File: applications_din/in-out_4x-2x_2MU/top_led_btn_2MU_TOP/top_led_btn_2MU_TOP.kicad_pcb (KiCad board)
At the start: 2 copper layers, 32 x 42 mm, 17 parts, among them J2 Conn_01x08_Pin, SW1 SW_PROG, SW2 SW_OUTA, SW3 SW_OUTB

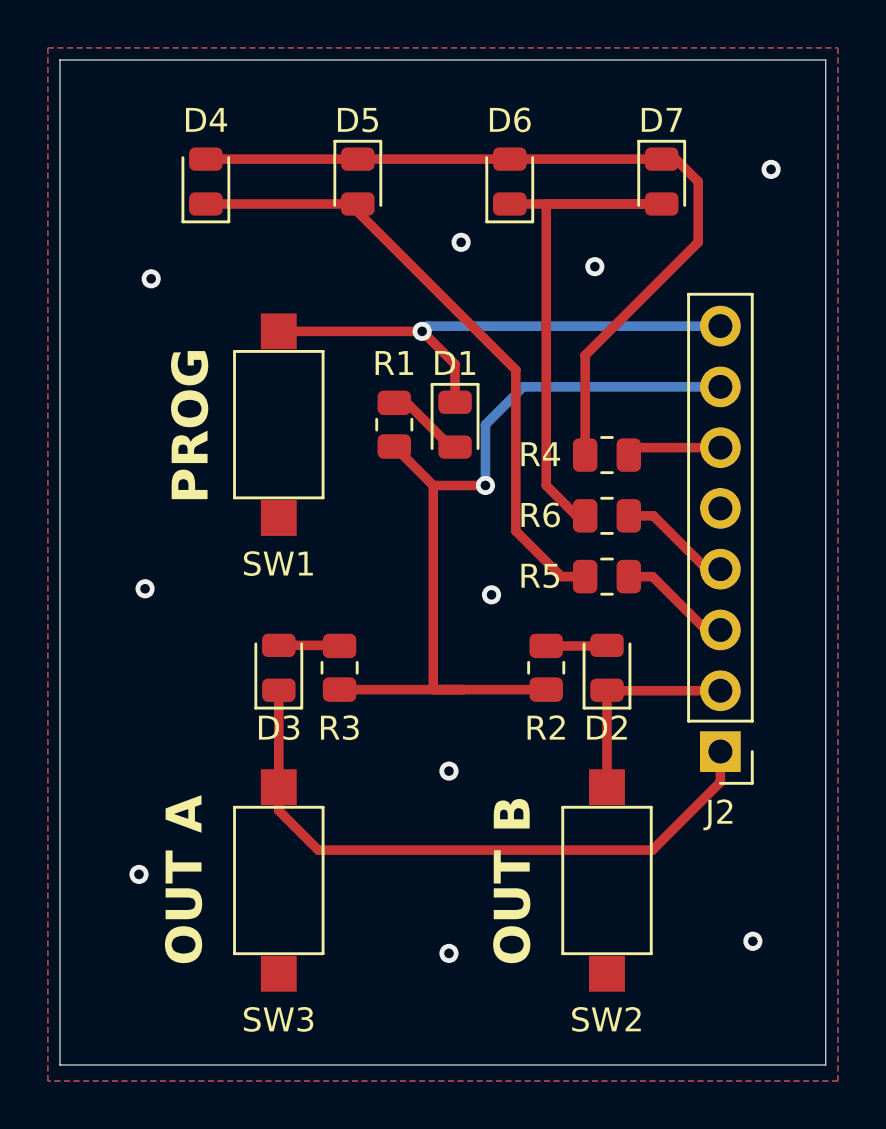
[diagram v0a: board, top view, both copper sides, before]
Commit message: properly rename 4in-2out application & top projects
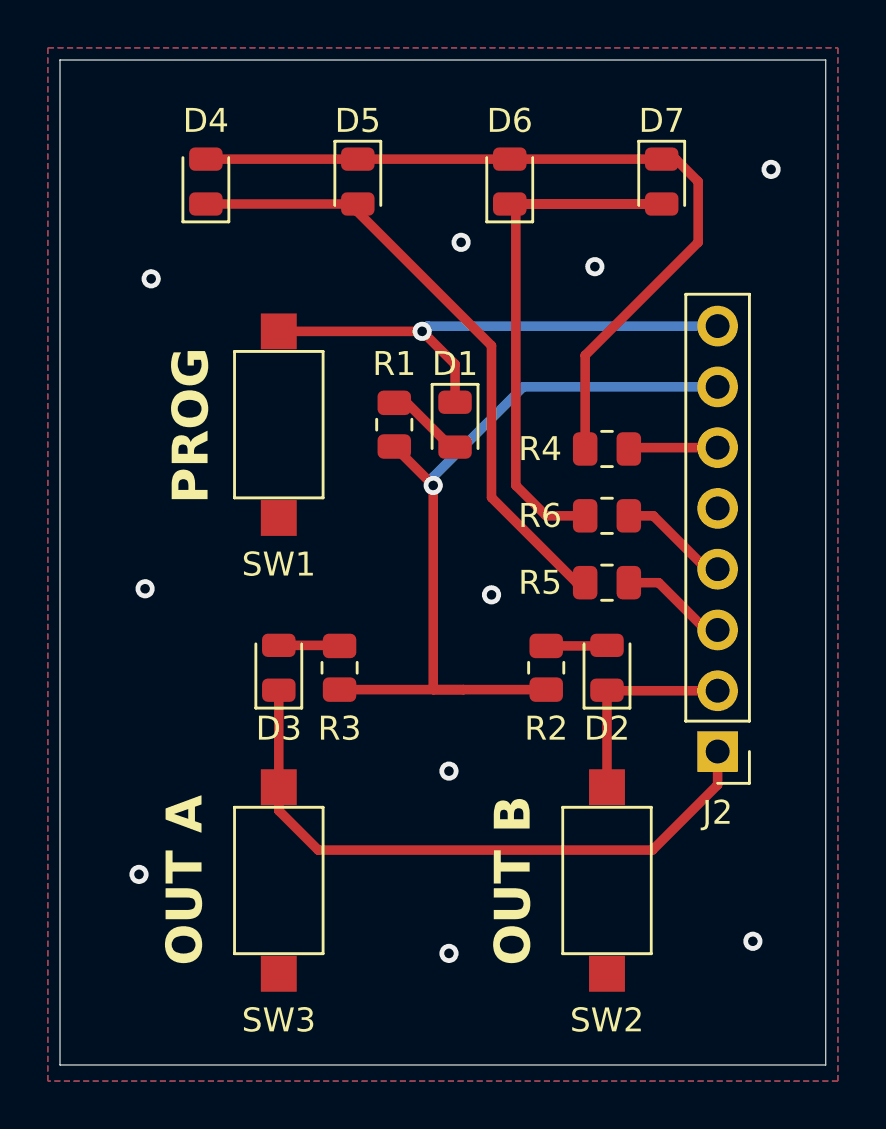
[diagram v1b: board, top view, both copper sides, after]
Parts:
- moved R4 0.25 mm to (121.9, 89.9)
- moved R5 0.25 mm to (121.9, 95.5)
- moved J2 0.12 mm to (126.5, 102.6)
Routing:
- net Net-(D6-K): track 25.1 -> 27.6 mm
- net +3V3: track 35.9 -> 34.5 mm
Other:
- board text added: "switch alternativ PTS636 SKG25J SMTR LFS https://eu.mouser.com/ProductDetail/CK/PTS636-SKG25J-SMTR-LFS"
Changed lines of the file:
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@@
 	(footprint "Resistor_SMD:R_0805_2012Metric"
 		(layer "F.Cu")
-		(at 121.92 90.17)
+		(at 121.92 89.916)
 		(descr "Resistor SMD 0805 (2012 Metric), square (rectangular) end terminal, IPC_7351 nominal, (Body size source: IPC-SM-782 page 72, https://www.pcb-3d.com/wordpress/wp-content/uploads/ipc-sm-782a_amendment_1_and_2.pdf), generated with kicad-footprint-generator")
 		(tags "resistor")
@@
 	(footprint "Resistor_SMD:R_0805_2012Metric"
 		(layer "F.Cu")
-		(at 121.92 95.25 180)
+		(at 121.92 95.504 180)
 		(descr "Resistor SMD 0805 (2012 Metric), square (rectangular) end terminal, IPC_7351 nominal, (Body size source: IPC-SM-782 page 72, https://www.pcb-3d.com/wordpress/wp-content/uploads/ipc-sm-782a_amendment_1_and_2.pdf), generated with kicad-footprint-generator")
 		(tags "resistor")
@@
 	(footprint "Connector_PinHeader_2.54mm:PinHeader_1x08_P2.54mm_Vertical"
 		(layer "F.Cu")
-		(at 126.66 102.56 180)
+		(at 126.5428 102.56 180)
 		(descr "Through hole straight pin header, 1x08, 2.54mm pitch, single row")
 		(tags "Through hole pin header THT 1x08 2.54mm single row")
@@
 		)
 	)
+	(gr_text "switch alternativ PTS636 SKG25J SMTR LFS\nhttps://eu.mouser.com/ProductDetail/CK/PTS636-SKG25J-SMTR-LFS"
+		(at 98.552 125.984 0)
+		(layer "Cmts.User")
+		(effects
+			(font
+				(size 1.5 1.5)
+				(thickness 0.3)
+				(bold yes)
+			)
+			(justify left bottom)
+		)
+	)
 	(segment
 		(start 115.40375 89.8375)
@@
 	)
 	(segment
-		(start 114.195 85)
-		(end 114.415 84.78)
+		(start 114.415 84.78)
+		(end 126.5428 84.78)
 		(width 0.4)
 		(layer "B.Cu")
@@
 	)
 	(segment
-		(start 114.415 84.78)
-		(end 126.66 84.78)
+		(start 114.195 85)
+		(end 114.415 84.78)
 		(width 0.4)
 		(layer "B.Cu")
@@
 	)
 	(segment
-		(start 121.9425 100.02)
+		(start 121.92 104.05)
 		(end 121.92 99.9975)
 		(width 0.4)
@@
 	)
 	(segment
-		(start 121.92 104.05)
+		(start 121.9425 100.02)
 		(end 121.92 99.9975)
 		(width 0.4)
@@
 	)
 	(segment
-		(start 126.66 100.02)
+		(start 126.5428 100.02)
 		(end 121.9425 100.02)
 		(width 0.4)
@@
 	)
 	(segment
-		(start 109.855 106.68)
-		(end 123.8175 106.68)
+		(start 126.5428 103.9547)
+		(end 126.5428 102.56)
 		(width 0.4)
 		(layer "F.Cu")
@@
 	)
 	(segment
-		(start 123.8175 106.68)
-		(end 126.66 103.8375)
+		(start 108.204 104.05)
+		(end 108.204 99.9975)
 		(width 0.4)
 		(layer "F.Cu")
@@
 	)
 	(segment
-		(start 126.66 103.8375)
-		(end 126.66 102.56)
+		(start 108.204 104.05)
+		(end 108.204 105.029)
 		(width 0.4)
 		(layer "F.Cu")
@@
 	)
 	(segment
-		(start 108.204 104.05)
-		(end 108.204 99.9975)
+		(start 108.204 105.029)
+		(end 109.855 106.68)
 		(width 0.4)
 		(layer "F.Cu")
@@
 	)
 	(segment
-		(start 108.204 105.029)
-		(end 109.855 106.68)
+		(start 123.8175 106.68)
+		(end 126.5428 103.9547)
 		(width 0.4)
 		(layer "F.Cu")
@@
 	)
 	(segment
-		(start 108.204 104.05)
-		(end 108.204 105.029)
+		(start 109.855 106.68)
+		(end 123.8175 106.68)
 		(width 0.4)
 		(layer "F.Cu")
@@
 	)
 	(segment
-		(start 125.73 81.28)
-		(end 125.73 78.74)
+		(start 117.856 77.8025)
+		(end 124.206 77.8025)
 		(width 0.4)
 		(layer "F.Cu")
@@
 	)
 	(segment
-		(start 117.856 77.8025)
-		(end 124.206 77.8025)
+		(start 125.73 81.28)
+		(end 125.73 78.74)
 		(width 0.4)
 		(layer "F.Cu")
@@
 	)
 	(segment
-		(start 125.73 78.74)
-		(end 124.7925 77.8025)
+		(start 121.0075 86.0025)
+		(end 125.73 81.28)
 		(width 0.4)
 		(layer "F.Cu")
@@
 	)
 	(segment
-		(start 121.0075 90.17)
+		(start 121.0075 89.916)
 		(end 121.0075 86.0025)
 		(width 0.4)
@@
 	)
 	(segment
-		(start 124.7925 77.8025)
-		(end 124.206 77.8025)
+		(start 125.73 78.74)
+		(end 124.7925 77.8025)
 		(width 0.4)
 		(layer "F.Cu")
@@
 	)
 	(segment
-		(start 121.0075 86.0025)
-		(end 125.73 81.28)
+		(start 124.7925 77.8025)
+		(end 124.206 77.8025)
 		(width 0.4)
 		(layer "F.Cu")
@@
 	)
 	(segment
-		(start 118.11 93.345)
-		(end 120.015 95.25)
+		(start 111.506 79.6775)
+		(end 111.506 80.01)
 		(width 0.4)
 		(layer "F.Cu")
@@
 	)
 	(segment
-		(start 111.506 79.6775)
-		(end 111.506 80.01)
+		(start 117.094 85.598)
+		(end 117.094 91.948)
 		(width 0.4)
 		(layer "F.Cu")
@@
 	)
 	(segment
-		(start 118.11 86.614)
-		(end 118.11 93.345)
+		(start 111.506 80.01)
+		(end 117.094 85.598)
 		(width 0.4)
 		(layer "F.Cu")
@@
 	)
 	(segment
-		(start 111.506 80.01)
-		(end 118.11 86.614)
+		(start 120.65 95.504)
+		(end 121.0075 95.504)
 		(width 0.4)
 		(layer "F.Cu")
@@
 	)
 	(segment
-		(start 120.015 95.25)
-		(end 121.0075 95.25)
+		(start 117.094 91.948)
+		(end 120.65 95.504)
 		(width 0.4)
 		(layer "F.Cu")
@@
 	)
 	(segment
-		(start 124.206 79.6775)
-		(end 119.38 79.6775)
+		(start 119.38 92.71)
+		(end 121.0075 92.71)
 		(width 0.4)
 		(layer "F.Cu")
@@
 	)
 	(segment
-		(start 119.38 91.44)
-		(end 120.65 92.71)
+		(start 118.11 79.6775)
+		(end 118.11 91.44)
 		(width 0.4)
 		(layer "F.Cu")
@@
 	)
 	(segment
-		(start 120.65 92.71)
-		(end 121.0075 92.71)
+		(start 118.11 91.44)
+		(end 119.38 92.71)
 		(width 0.4)
 		(layer "F.Cu")
@@
 	)
 	(segment
-		(start 119.38 79.6775)
-		(end 119.38 91.44)
+		(start 117.856 79.6775)
+		(end 124.206 79.6775)
 		(width 0.4)
 		(layer "F.Cu")
@@
 	)
 	(segment
-		(start 117.856 79.6775)
-		(end 124.206 79.6775)
+		(start 124.206 79.6775)
+		(end 118.11 79.6775)
 		(width 0.4)
 		(layer "F.Cu")
@@
 	)
 	(segment
-		(start 126.089688 94.94)
-		(end 123.859688 92.71)
+		(start 123.859688 92.71)
+		(end 122.8325 92.71)
 		(width 0.4)
 		(layer "F.Cu")
@@
 	)
 	(segment
-		(start 126.66 94.94)
+		(start 126.5428 94.94)
 		(end 126.089688 94.94)
 		(width 0.4)
@@
 	)
 	(segment
-		(start 123.859688 92.71)
-		(end 122.8325 92.71)
+		(start 126.089688 94.94)
+		(end 123.859688 92.71)
 		(width 0.4)
 		(layer "F.Cu")
@@
 	)
 	(segment
-		(start 123.1425 89.86)
-		(end 126.66 89.86)
+		(start 122.8325 89.916)
+		(end 122.8885 89.86)
 		(width 0.4)
 		(layer "F.Cu")
@@
 	)
 	(segment
-		(start 122.8325 90.17)
-		(end 123.1425 89.86)
+		(start 122.8885 89.86)
+		(end 126.5428 89.86)
 		(width 0.4)
 		(layer "F.Cu")
@@
 	)
 	(segment
-		(start 116.84 91.44)
-		(end 114.6575 91.44)
-		(width 0.4)
-		(layer "F.Cu")
-		(net 13)
-	)
-	(segment
 		(start 115.9275 99.9725)
 		(end 114.6575 99.9725)
@@
 	)
 	(via
-		(at 116.84 91.44)
+		(at 114.6575 91.44)
 		(size 0.8)
 		(drill 0.4)
@@
 	)
 	(segment
-		(start 116.84 88.9)
+		(start 114.6575 91.0825)
 		(end 118.42 87.32)
 		(width 0.4)
@@
 	)
 	(segment
-		(start 118.42 87.32)
-		(end 126.66 87.32)
+		(start 114.6575 91.44)
+		(end 114.6575 91.0825)
 		(width 0.4)
 		(layer "B.Cu")
@@
 	)
 	(segment
-		(start 116.84 91.44)
-		(end 116.84 88.9)
+		(start 118.42 87.32)
+		(end 126.5428 87.32)
 		(width 0.4)
 		(layer "B.Cu")
@@
 	)
 	(segment
-		(start 126.66 97.48)
-		(end 126.055 97.48)
+		(start 124.079 95.504)
+		(end 122.8325 95.504)
 		(width 0.4)
 		(layer "F.Cu")
@@
 	)
 	(segment
-		(start 123.825 95.25)
-		(end 122.8325 95.25)
+		(start 126.055 97.48)
+		(end 124.079 95.504)
 		(width 0.4)
 		(layer "F.Cu")
@@
 	)
 	(segment
-		(start 126.055 97.48)
-		(end 123.825 95.25)
+		(start 126.5428 97.48)
+		(end 126.055 97.48)
 		(width 0.4)
 		(layer "F.Cu")

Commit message: update in-out_4x-2x_2MU - final for now
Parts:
- SW1, SW2, SW3: footprint Button_Switch_SMD:SW_SPST_CK_RS282G05A3 -> Button_Switch_SMD:SW_SPST_Omron_B3FS-100xP
- moved D1 2.27 mm to (114.6, 86.9), turned to 0 degrees
- moved R1 1.61 mm to (114.6, 89.4), turned to 180 degrees
- moved SW1 0.76 mm to (109.0, 88.9)
- moved SW2 0.76 mm to (121.2, 108.0), turned to -90 degrees
- moved SW3 0.76 mm to (109.0, 108.0), turned to -90 degrees
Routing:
- net Net-(D1-K): track 22.0 -> 17.4 mm
- net Net-(D3-K): track 26.6 -> 28.8 mm
- net Net-(D2-K): track 8.68 -> 9.83 mm
